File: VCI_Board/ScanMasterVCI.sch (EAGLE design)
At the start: 82 parts, among them IC1 XMEGA16A4A, Q1 MMBT4403, Q10 ZXMP6A17G, Q2 MMBT3904, Q3 MMBT3904, Q4 MMBT3904, Q5 MMBT3904, Q6 MMBT3904, Q7 NTZD5110N, Q8 NTZD5110N, Q9 NTZD5110N, U1 L78L08ABUTR, U2 ISO1050, U3 SN65HVDA195-Q1, U4 MAX17502EATB+, U5 MAX17502FATB+

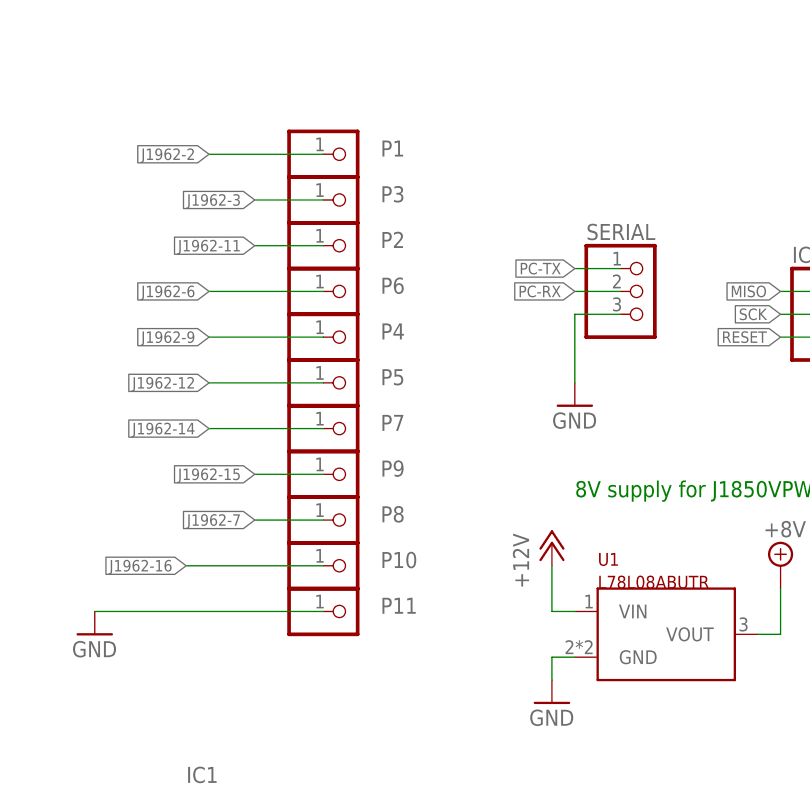
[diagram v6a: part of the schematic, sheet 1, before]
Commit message: Widened +12V trace, re-named pins
I had ran a part renaming script before and forgot to change the names of the OBD  pins back to what they're supposed to be.
I'm not sure if it's necessary, but I'm making the trace for the +12v rail significantly wider, since it will carry the most current. At this point I'm unsure if I need to do this to the 3.3 and 5v rails.
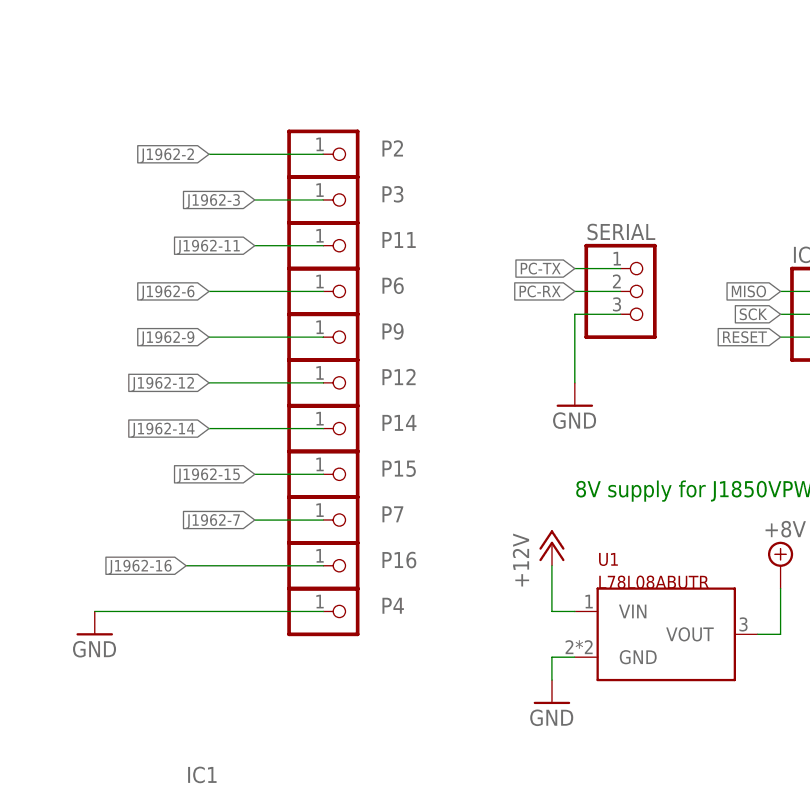
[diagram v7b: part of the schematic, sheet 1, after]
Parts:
- removed P1, P8: (no value), pinhead:PINHD-1X1
- added P14, P15: (no value), pinhead:PINHD-1X1
- renumbered P10 to P16, P5 to P12
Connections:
- net GND: now also P4.1; no longer P11.1
- net J1962-11: now also P11.1; no longer P2.1
- net J1962-14: now also P14.1; no longer P7.1
- net J1962-15: now also P15.1; no longer P9.1
- net J1962-2: now also P2.1; no longer P1.1
- net J1962-7: now also P7.1; no longer P8.1
- net J1962-9: now also P9.1; no longer P4.1
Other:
- moved on the sheet: P11, P2, P4, P7, P9
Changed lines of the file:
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@@
 <clearance class="0" value="0.1524"/>
 </class>
-<class number="1" name="+12v" width="0.2032" drill="0.3048">
+<class number="1" name="+12v" width="0.3048" drill="0.3048">
 <clearance class="1" value="0.1524"/>
 </class>
@@
 <part name="+3V8" library="supply1" library_urn="urn:adsk.eagle:library:371" deviceset="+3V3" device=""/>
 <part name="SERIAL" library="pinhead" library_urn="urn:adsk.eagle:library:325" deviceset="PINHD-1X3" device="" package3d_urn="urn:adsk.eagle:package:22458/2"/>
-<part name="P1" library="pinhead" library_urn="urn:adsk.eagle:library:325" deviceset="PINHD-1X1" device="" package3d_urn="urn:adsk.eagle:package:22485/1"/>
+<part name="P2" library="pinhead" library_urn="urn:adsk.eagle:library:325" deviceset="PINHD-1X1" device="" package3d_urn="urn:adsk.eagle:package:22485/1"/>
 <part name="P3" library="pinhead" library_urn="urn:adsk.eagle:library:325" deviceset="PINHD-1X1" device="" package3d_urn="urn:adsk.eagle:package:22485/1"/>
-<part name="P11" library="pinhead" library_urn="urn:adsk.eagle:library:325" deviceset="PINHD-1X1" device="" package3d_urn="urn:adsk.eagle:package:22485/1"/>
+<part name="P4" library="pinhead" library_urn="urn:adsk.eagle:library:325" deviceset="PINHD-1X1" device="" package3d_urn="urn:adsk.eagle:package:22485/1"/>
 <part name="P6" library="pinhead" library_urn="urn:adsk.eagle:library:325" deviceset="PINHD-1X1" device="" package3d_urn="urn:adsk.eagle:package:22485/1"/>
-<part name="P8" library="pinhead" library_urn="urn:adsk.eagle:library:325" deviceset="PINHD-1X1" device="" package3d_urn="urn:adsk.eagle:package:22485/1"/>
-<part name="P4" library="pinhead" library_urn="urn:adsk.eagle:library:325" deviceset="PINHD-1X1" device="" package3d_urn="urn:adsk.eagle:package:22485/1"/>
-<part name="P2" library="pinhead" library_urn="urn:adsk.eagle:library:325" deviceset="PINHD-1X1" device="" package3d_urn="urn:adsk.eagle:package:22485/1"/>
 <part name="P7" library="pinhead" library_urn="urn:adsk.eagle:library:325" deviceset="PINHD-1X1" device="" package3d_urn="urn:adsk.eagle:package:22485/1"/>
 <part name="P9" library="pinhead" library_urn="urn:adsk.eagle:library:325" deviceset="PINHD-1X1" device="" package3d_urn="urn:adsk.eagle:package:22485/1"/>
-<part name="P10" library="pinhead" library_urn="urn:adsk.eagle:library:325" deviceset="PINHD-1X1" device="" package3d_urn="urn:adsk.eagle:package:22485/1"/>
-<part name="P5" library="pinhead" library_urn="urn:adsk.eagle:library:325" deviceset="PINHD-1X1" device="" package3d_urn="urn:adsk.eagle:package:22485/1"/>
+<part name="P11" library="pinhead" library_urn="urn:adsk.eagle:library:325" deviceset="PINHD-1X1" device="" package3d_urn="urn:adsk.eagle:package:22485/1"/>
+<part name="P14" library="pinhead" library_urn="urn:adsk.eagle:library:325" deviceset="PINHD-1X1" device="" package3d_urn="urn:adsk.eagle:package:22485/1"/>
+<part name="P15" library="pinhead" library_urn="urn:adsk.eagle:library:325" deviceset="PINHD-1X1" device="" package3d_urn="urn:adsk.eagle:package:22485/1"/>
+<part name="P16" library="pinhead" library_urn="urn:adsk.eagle:library:325" deviceset="PINHD-1X1" device="" package3d_urn="urn:adsk.eagle:package:22485/1"/>
+<part name="P12" library="pinhead" library_urn="urn:adsk.eagle:library:325" deviceset="PINHD-1X1" device="" package3d_urn="urn:adsk.eagle:package:22485/1"/>
 <part name="Q7" library="customics" deviceset="NTZD5110N" device=""/>
 <part name="Q8" library="customics" deviceset="NTZD5110N" device=""/>
@@
 <instance part="+3V8" gate="G$1" x="106.68" y="154.94"/>
 <instance part="SERIAL" gate="A" x="73.66" y="147.32"/>
-<instance part="P1" gate="G$1" x="40.64" y="162.56" smashed="yes">
+<instance part="P2" gate="G$1" x="40.64" y="162.56" smashed="yes">
 <attribute name="NAME" x="44.45" y="163.195" size="1.778" layer="95" align="center-left"/>
 <attribute name="VALUE" x="34.29" y="157.48" size="1.778" layer="96"/>
@@
 <attribute name="VALUE" x="34.29" y="152.4" size="1.778" layer="96"/>
 </instance>
-<instance part="P11" gate="G$1" x="40.64" y="111.76" smashed="yes">
+<instance part="P4" gate="G$1" x="40.64" y="111.76" smashed="yes">
 <attribute name="NAME" x="44.45" y="112.395" size="1.778" layer="95" align="center-left"/>
 <attribute name="VALUE" x="34.29" y="106.68" size="1.778" layer="96"/>
@@
 <attribute name="VALUE" x="34.29" y="142.24" size="1.778" layer="96"/>
 </instance>
-<instance part="P8" gate="G$1" x="40.64" y="121.92" smashed="yes">
+<instance part="P7" gate="G$1" x="40.64" y="121.92" smashed="yes">
 <attribute name="NAME" x="44.45" y="122.555" size="1.778" layer="95" align="center-left"/>
 <attribute name="VALUE" x="34.29" y="116.84" size="1.778" layer="96"/>
 </instance>
-<instance part="P4" gate="G$1" x="40.64" y="142.24" smashed="yes">
+<instance part="P9" gate="G$1" x="40.64" y="142.24" smashed="yes">
 <attribute name="NAME" x="44.45" y="142.875" size="1.778" layer="95" align="center-left"/>
 <attribute name="VALUE" x="34.29" y="137.16" size="1.778" layer="96"/>
 </instance>
-<instance part="P2" gate="G$1" x="40.64" y="152.4" smashed="yes">
+<instance part="P11" gate="G$1" x="40.64" y="152.4" smashed="yes">
 <attribute name="NAME" x="44.45" y="153.035" size="1.778" layer="95" align="center-left"/>
 <attribute name="VALUE" x="34.29" y="147.32" size="1.778" layer="96"/>
 </instance>
-<instance part="P7" gate="G$1" x="40.64" y="132.08" smashed="yes">
+<instance part="P14" gate="G$1" x="40.64" y="132.08" smashed="yes">
 <attribute name="NAME" x="44.45" y="132.715" size="1.778" layer="95" align="center-left"/>
 <attribute name="VALUE" x="34.29" y="127" size="1.778" layer="96"/>
 </instance>
-<instance part="P9" gate="G$1" x="40.64" y="127" smashed="yes">
+<instance part="P15" gate="G$1" x="40.64" y="127" smashed="yes">
 <attribute name="NAME" x="44.45" y="127.635" size="1.778" layer="95" align="center-left"/>
 <attribute name="VALUE" x="34.29" y="121.92" size="1.778" layer="96"/>
 </instance>
-<instance part="P10" gate="G$1" x="40.64" y="116.84" smashed="yes">
+<instance part="P16" gate="G$1" x="40.64" y="116.84" smashed="yes">
 <attribute name="NAME" x="44.45" y="117.475" size="1.778" layer="95" align="center-left"/>
 <attribute name="VALUE" x="34.29" y="111.76" size="1.778" layer="96"/>
 </instance>
-<instance part="P5" gate="G$1" x="40.64" y="137.16" smashed="yes">
+<instance part="P12" gate="G$1" x="40.64" y="137.16" smashed="yes">
 <attribute name="NAME" x="44.45" y="137.795" size="1.778" layer="95" align="center-left"/>
 <attribute name="VALUE" x="34.29" y="132.08" size="1.778" layer="96"/>
@@
 <wire x1="38.1" y1="111.76" x2="12.7" y2="111.76" width="0.1524" layer="91"/>
 <pinref part="GND46" gate="1" pin="GND"/>
-<pinref part="P11" gate="G$1" pin="1"/>
+<pinref part="P4" gate="G$1" pin="1"/>
 </segment>
 <segment>
@@
 <wire x1="38.1" y1="116.84" x2="22.86" y2="116.84" width="0.1524" layer="91"/>
 <label x="22.86" y="116.84" size="1.27" layer="95" rot="R180" xref="yes"/>
-<pinref part="P10" gate="G$1" pin="1"/>
+<pinref part="P16" gate="G$1" pin="1"/>
 </segment>
 </net>
@@
 <wire x1="38.1" y1="127" x2="30.48" y2="127" width="0.1524" layer="91"/>
 <label x="30.48" y="127" size="1.27" layer="95" rot="R180" xref="yes"/>
-<pinref part="P9" gate="G$1" pin="1"/>
+<pinref part="P15" gate="G$1" pin="1"/>
 </segment>
 </net>
@@
 <wire x1="38.1" y1="121.92" x2="30.48" y2="121.92" width="0.1524" layer="91"/>
 <label x="30.48" y="121.92" size="1.27" layer="95" rot="R180" xref="yes"/>
-<pinref part="P8" gate="G$1" pin="1"/>
+<pinref part="P7" gate="G$1" pin="1"/>
 </segment>
 </net>
@@
 <wire x1="38.1" y1="137.16" x2="25.4" y2="137.16" width="0.1524" layer="91"/>
 <label x="25.4" y="137.16" size="1.27" layer="95" rot="R180" xref="yes"/>
-<pinref part="P5" gate="G$1" pin="1"/>
+<pinref part="P12" gate="G$1" pin="1"/>
 </segment>
 </net>
@@
 <wire x1="38.1" y1="132.08" x2="25.4" y2="132.08" width="0.1524" layer="91"/>
 <label x="25.4" y="132.08" size="1.27" layer="95" rot="R180" xref="yes"/>
-<pinref part="P7" gate="G$1" pin="1"/>
+<pinref part="P14" gate="G$1" pin="1"/>
 </segment>
 </net>
@@
 <wire x1="38.1" y1="142.24" x2="25.4" y2="142.24" width="0.1524" layer="91"/>
 <label x="25.4" y="142.24" size="1.27" layer="95" rot="R180" xref="yes"/>
-<pinref part="P4" gate="G$1" pin="1"/>
+<pinref part="P9" gate="G$1" pin="1"/>
 </segment>
 </net>
@@
 <wire x1="38.1" y1="152.4" x2="30.48" y2="152.4" width="0.1524" layer="91"/>
 <label x="30.48" y="152.4" size="1.27" layer="95" rot="R180" xref="yes"/>
-<pinref part="P2" gate="G$1" pin="1"/>
+<pinref part="P11" gate="G$1" pin="1"/>
 </segment>
 </net>
@@
 <wire x1="38.1" y1="162.56" x2="25.4" y2="162.56" width="0.1524" layer="91"/>
 <label x="25.4" y="162.56" size="1.27" layer="95" rot="R180" xref="yes"/>
-<pinref part="P1" gate="G$1" pin="1"/>
-</segment>
-</net>
+<pinref part="P2" gate="G$1" pin="1"/>
+</segment>
+</net>
